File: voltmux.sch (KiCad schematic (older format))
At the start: 32 parts, among them J2 Conn_02x07_Counter_Clockwise, U10 CD74HC4067SM

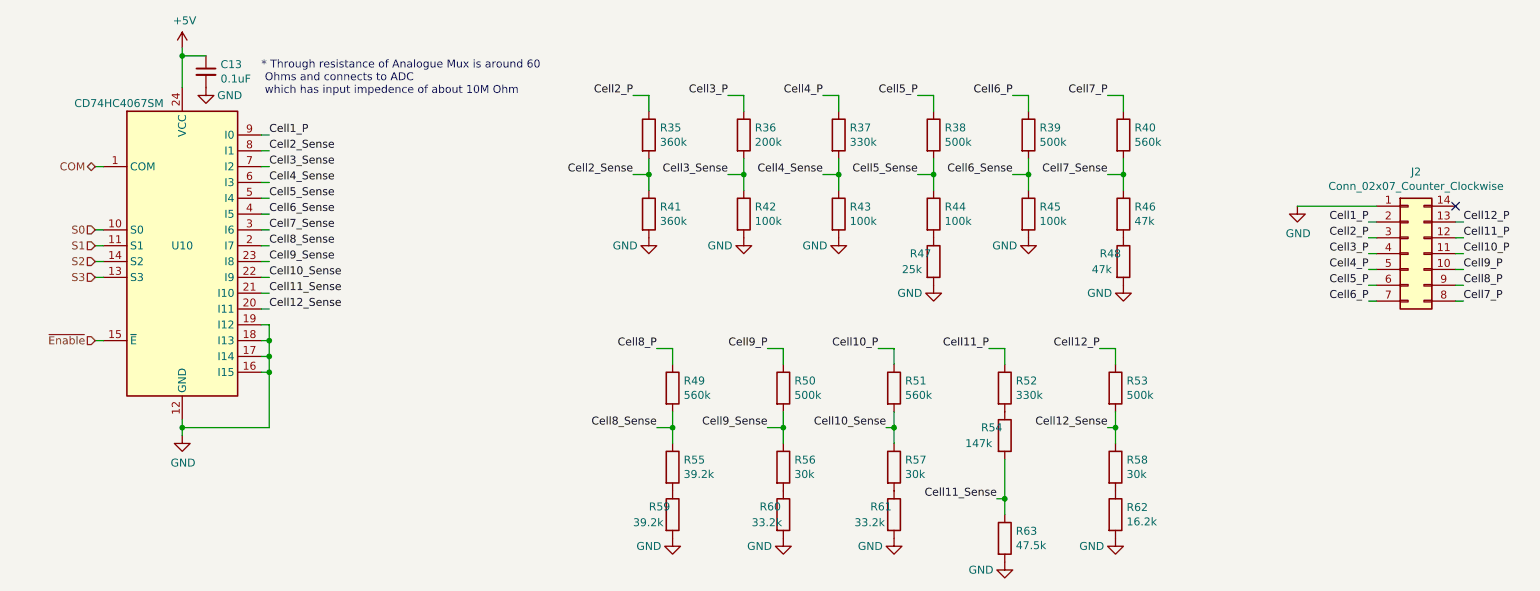
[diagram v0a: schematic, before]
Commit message: Switched to lower GPIO pin part to save space
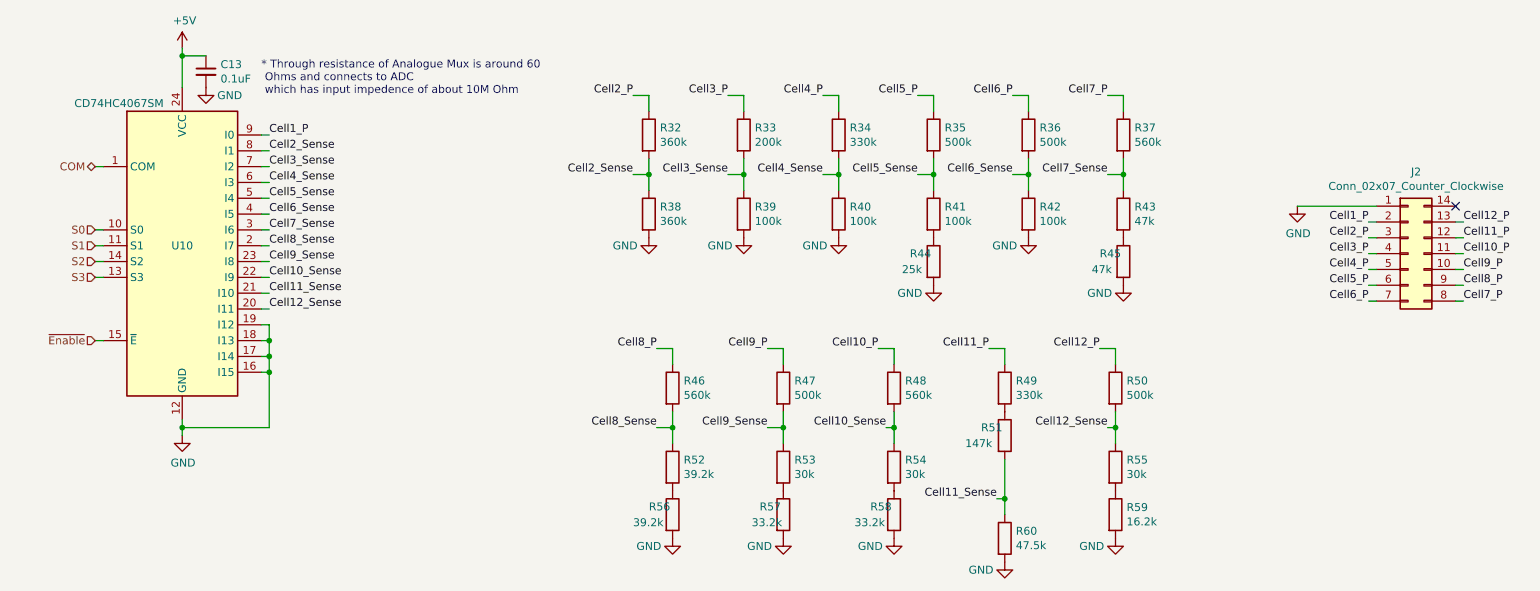
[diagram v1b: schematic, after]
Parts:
- renumbered R35 to R32, R36 to R33, R37 to R34, R38 to R35, R39 to R36, R40 to R37, R41 to R38, R42 to R39, R43 to R40, R44 to R41, R45 to R42, R46 to R43, R47 to R44, R48 to R45, R49 to R46, R50 to R47, R51 to R48, R52 to R49, R53 to R50, R54 to R51, R55 to R52, R56 to R53, R57 to R54, R58 to R55, R59 to R56, R60 to R57, R61 to R58, R62 to R59, R63 to R60

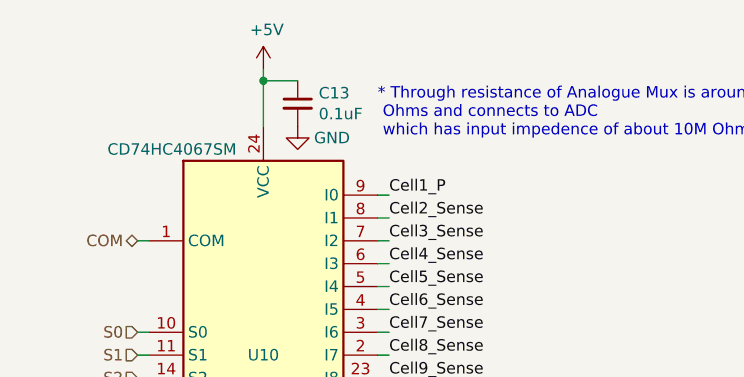
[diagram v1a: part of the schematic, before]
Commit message: Removed SD card Adapter, added programming port
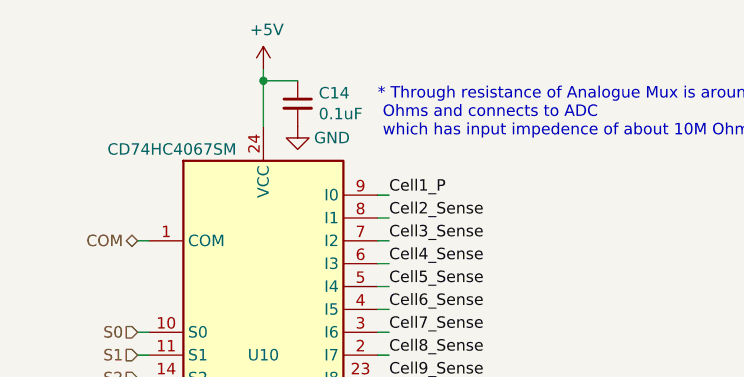
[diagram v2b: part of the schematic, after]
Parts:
- renumbered C13 to C14
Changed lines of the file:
@@
 	2350 3550 2350 3500
 $Comp
-L Device:C_Small C13
+L Device:C_Small C14
 U 1 1 5F5548EC
 P 2500 1250
-F 0 "C13" H 2592 1296 50  0000 L CNN
+F 0 "C14" H 2592 1296 50  0000 L CNN
 F 1 "0.1uF" H 2592 1205 50  0000 L CNN
 F 2 "Capacitor_SMD:C_1206_3216Metric" H 2500 1250 50  0001 C CNN

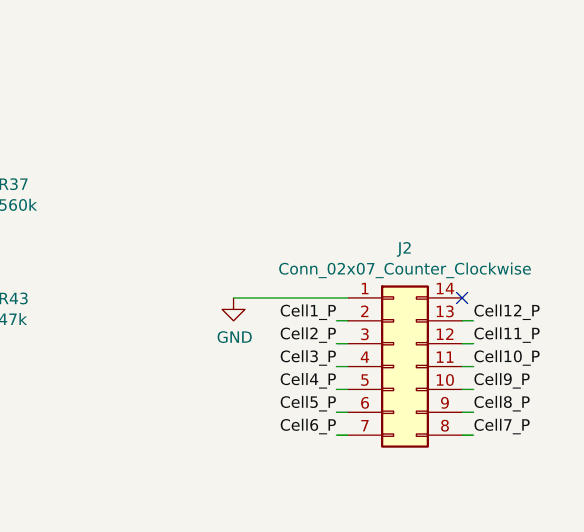
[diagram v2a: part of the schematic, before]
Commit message: Added ext ADC pin and fixed connection bugs
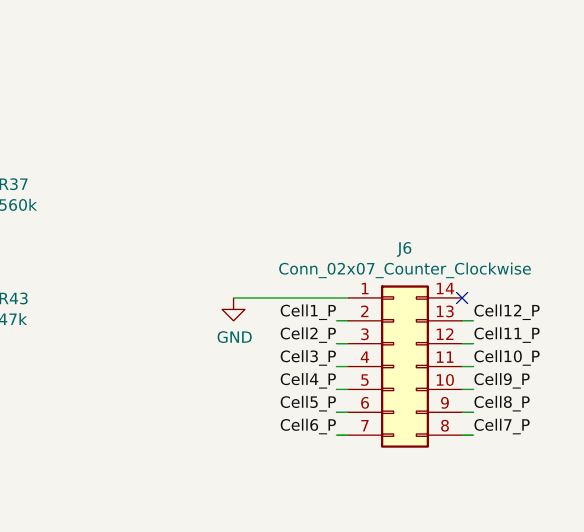
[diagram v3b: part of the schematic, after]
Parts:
- renumbered J2 to J6
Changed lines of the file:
@@
 $EndComp
 $Comp
-L power:GND #PWR055
+L power:GND #PWR057
 U 1 1 5F55349E
 P 2350 3550
-F 0 "#PWR055" H 2350 3300 50  0001 C CNN
+F 0 "#PWR057" H 2350 3300 50  0001 C CNN
 F 1 "GND" H 2355 3377 50  0000 C CNN
 F 2 "" H 2350 3550 50  0001 C CNN
@@
 $EndComp
 $Comp
-L power:GND #PWR047
+L power:GND #PWR049
 U 1 1 5F55509A
 P 2500 1350
-F 0 "#PWR047" H 2500 1100 50  0001 C CNN
+F 0 "#PWR049" H 2500 1100 50  0001 C CNN
 F 1 "GND" H 2650 1300 50  0000 C CNN
 F 2 "" H 2500 1350 50  0001 C CNN
@@
 $EndComp
 $Comp
-L power:+5V #PWR046
+L power:+5V #PWR048
 U 1 1 5F55562D
 P 2350 1100
-F 0 "#PWR046" H 2350 950 50  0001 C CNN
+F 0 "#PWR048" H 2350 950 50  0001 C CNN
 F 1 "+5V" H 2365 1273 50  0000 C CNN
 F 2 "" H 2350 1100 50  0001 C CNN
@@
 	2350 1150 2350 1350
 $Comp
-L power:GND #PWR048
+L power:GND #PWR050
 U 1 1 5F55CE43
 P 9400 2100
-F 0 "#PWR048" H 9400 1850 50  0001 C CNN
+F 0 "#PWR050" H 9400 1850 50  0001 C CNN
 F 1 "GND" H 9405 1927 50  0000 C CNN
 F 2 "" H 9400 2100 50  0001 C CNN
@@
 Cell6_P
 $Comp
-L Connector_Generic:Conn_02x07_Counter_Clockwise J2
+L Connector_Generic:Conn_02x07_Counter_Clockwise J6
 U 1 1 5F55EF88
 P 10100 2400
-F 0 "J2" H 10150 2917 50  0000 C CNN
+F 0 "J6" H 10150 2917 50  0000 C CNN
 F 1 "Conn_02x07_Counter_Clockwise" H 10150 2826 50  0000 C CNN
 F 2 "Connector_PinHeader_2.54mm:PinHeader_2x07_P2.54mm_Vertical" H 10100 2400 50  0001 C CNN
@@
 	8250 3000 8250 3100
 $Comp
-L power:GND #PWR049
+L power:GND #PWR051
 U 1 1 5F58E473
 P 5300 2300
-F 0 "#PWR049" H 5300 2050 50  0001 C CNN
+F 0 "#PWR051" H 5300 2050 50  0001 C CNN
 F 1 "GND" H 5150 2250 50  0000 C CNN
 F 2 "" H 5300 2300 50  0001 C CNN
@@
 $EndComp
 $Comp
-L power:GND #PWR050
+L power:GND #PWR052
 U 1 1 5F58E961
 P 5900 2300
-F 0 "#PWR050" H 5900 2050 50  0001 C CNN
+F 0 "#PWR052" H 5900 2050 50  0001 C CNN
 F 1 "GND" H 5750 2250 50  0000 C CNN
 F 2 "" H 5900 2300 50  0001 C CNN
@@
 $EndComp
 $Comp
-L power:GND #PWR051
+L power:GND #PWR053
 U 1 1 5F58EB9B
 P 6500 2300
-F 0 "#PWR051" H 6500 2050 50  0001 C CNN
+F 0 "#PWR053" H 6500 2050 50  0001 C CNN
 F 1 "GND" H 6350 2250 50  0000 C CNN
 F 2 "" H 6500 2300 50  0001 C CNN
@@
 $EndComp
 $Comp
-L power:GND #PWR052
+L power:GND #PWR054
 U 1 1 5F58EF8D
 P 7700 2300
-F 0 "#PWR052" H 7700 2050 50  0001 C CNN
+F 0 "#PWR054" H 7700 2050 50  0001 C CNN
 F 1 "GND" H 7550 2250 50  0000 C CNN
 F 2 "" H 7700 2300 50  0001 C CNN
@@
 $EndComp
 $Comp
-L power:GND #PWR060
+L power:GND #PWR062
 U 1 1 5F58FB94
 P 7550 4350
-F 0 "#PWR060" H 7550 4100 50  0001 C CNN
+F 0 "#PWR062" H 7550 4100 50  0001 C CNN
 F 1 "GND" H 7400 4300 50  0000 C CNN
 F 2 "" H 7550 4350 50  0001 C CNN
@@
 $EndComp
 $Comp
-L power:GND #PWR058
+L power:GND #PWR060
 U 1 1 5F627115
 P 6850 4200
-F 0 "#PWR058" H 6850 3950 50  0001 C CNN
+F 0 "#PWR060" H 6850 3950 50  0001 C CNN
 F 1 "GND" H 6700 4150 50  0000 C CNN
 F 2 "" H 6850 4200 50  0001 C CNN
@@
 $EndComp
 $Comp
-L power:GND #PWR057
+L power:GND #PWR059
 U 1 1 5F6278F7
 P 6150 4200
-F 0 "#PWR057" H 6150 3950 50  0001 C CNN
+F 0 "#PWR059" H 6150 3950 50  0001 C CNN
 F 1 "GND" H 6000 4150 50  0000 C CNN
 F 2 "" H 6150 4200 50  0001 C CNN
@@
 $EndComp
 $Comp
-L power:GND #PWR056
+L power:GND #PWR058
 U 1 1 5F627F6F
 P 5450 4200
-F 0 "#PWR056" H 5450 3950 50  0001 C CNN
+F 0 "#PWR058" H 5450 3950 50  0001 C CNN
 F 1 "GND" H 5300 4150 50  0000 C CNN
 F 2 "" H 5450 4200 50  0001 C CNN
@@
 $EndComp
 $Comp
-L power:GND #PWR059
+L power:GND #PWR061
 U 1 1 5F638E0E
 P 8250 4200
-F 0 "#PWR059" H 8250 3950 50  0001 C CNN
+F 0 "#PWR061" H 8250 3950 50  0001 C CNN
 F 1 "GND" H 8100 4150 50  0000 C CNN
 F 2 "" H 8250 4200 50  0001 C CNN
@@
 Connection ~ 7550 3950
 $Comp
-L power:GND #PWR053
+L power:GND #PWR055
 U 1 1 5F6490F9
 P 7100 2600
-F 0 "#PWR053" H 7100 2350 50  0001 C CNN
+F 0 "#PWR055" H 7100 2350 50  0001 C CNN
 F 1 "GND" H 6950 2550 50  0000 C CNN
 F 2 "" H 7100 2600 50  0001 C CNN
@@
 $EndComp
 $Comp
-L power:GND #PWR054
+L power:GND #PWR056
 U 1 1 5F64935A
 P 8300 2600
-F 0 "#PWR054" H 8300 2350 50  0001 C CNN
+F 0 "#PWR056" H 8300 2350 50  0001 C CNN
 F 1 "GND" H 8150 2550 50  0000 C CNN
 F 2 "" H 8300 2600 50  0001 C CNN

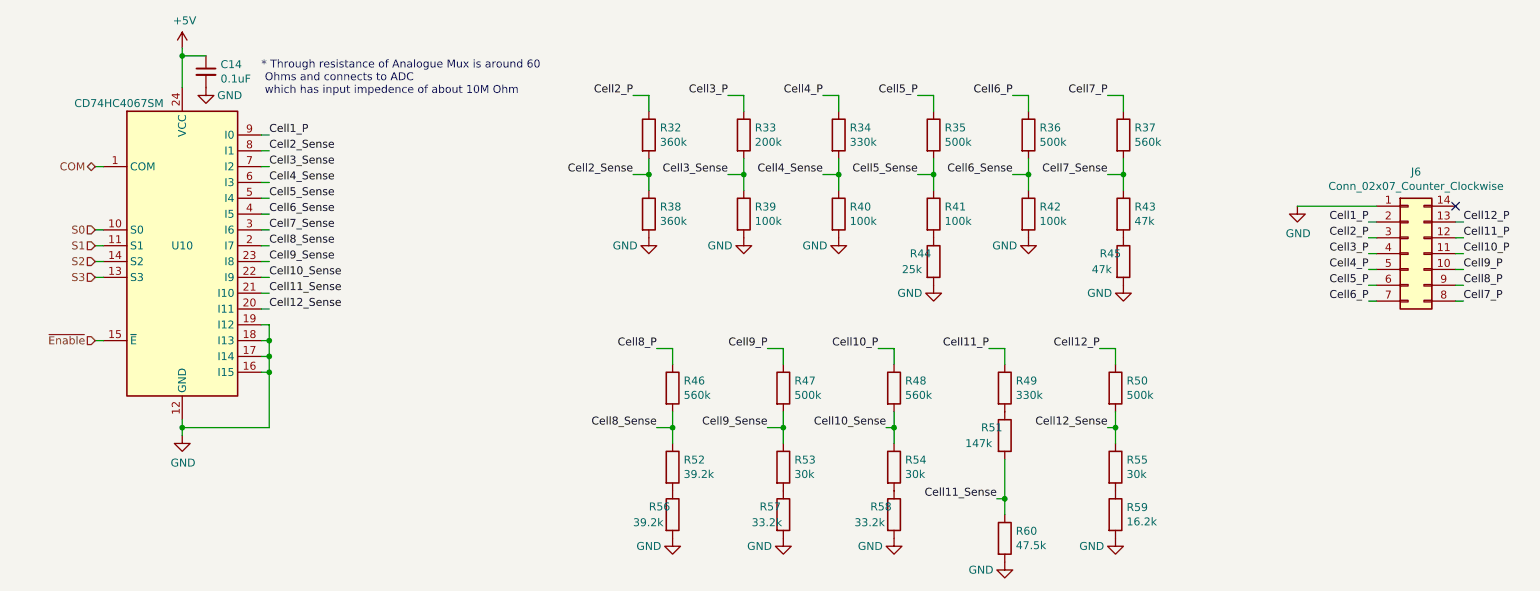
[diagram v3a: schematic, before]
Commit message: Added JST power connect and fixed some footprints
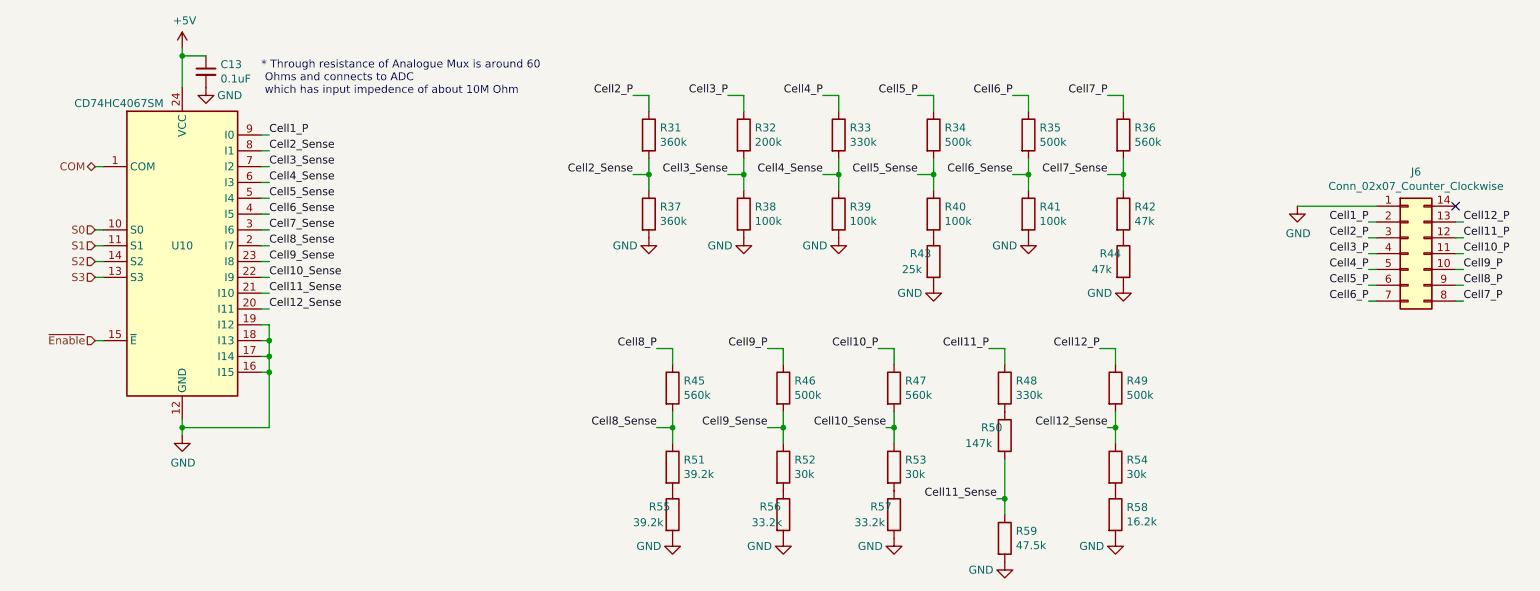
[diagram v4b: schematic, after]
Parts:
- renumbered C14 to C13, R32 to R31, R33 to R32, R34 to R33, R35 to R34, R36 to R35, R37 to R36, R38 to R37, R39 to R38, R40 to R39, R41 to R40, R42 to R41, R43 to R42, R44 to R43, R45 to R44, R46 to R45, R47 to R46, R48 to R47, R49 to R48, R50 to R49, R51 to R50, R52 to R51, R53 to R52, R54 to R53, R55 to R54, R56 to R55, R57 to R56, R58 to R57, R59 to R58, R60 to R59

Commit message: Refactored some naming
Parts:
- renumbered J6 to J5
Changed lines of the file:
@@
 $EndComp
 $Comp
-L power:GND #PWR055
+L power:GND #PWR054
 U 1 1 5F55349E
 P 2350 3550
-F 0 "#PWR055" H 2350 3300 50  0001 C CNN
+F 0 "#PWR054" H 2350 3300 50  0001 C CNN
 F 1 "GND" H 2355 3377 50  0000 C CNN
 F 2 "" H 2350 3550 50  0001 C CNN
@@
 $EndComp
 $Comp
-L power:GND #PWR047
+L power:GND #PWR046
 U 1 1 5F55509A
 P 2500 1350
-F 0 "#PWR047" H 2500 1100 50  0001 C CNN
+F 0 "#PWR046" H 2500 1100 50  0001 C CNN
 F 1 "GND" H 2650 1300 50  0000 C CNN
 F 2 "" H 2500 1350 50  0001 C CNN
@@
 $EndComp
 $Comp
-L power:+5V #PWR046
+L power:+5V #PWR045
 U 1 1 5F55562D
 P 2350 1100
-F 0 "#PWR046" H 2350 950 50  0001 C CNN
+F 0 "#PWR045" H 2350 950 50  0001 C CNN
 F 1 "+5V" H 2365 1273 50  0000 C CNN
 F 2 "" H 2350 1100 50  0001 C CNN
@@
 	2350 1150 2350 1350
 $Comp
-L power:GND #PWR048
+L power:GND #PWR047
 U 1 1 5F55CE43
 P 9400 2100
-F 0 "#PWR048" H 9400 1850 50  0001 C CNN
+F 0 "#PWR047" H 9400 1850 50  0001 C CNN
 F 1 "GND" H 9405 1927 50  0000 C CNN
 F 2 "" H 9400 2100 50  0001 C CNN
@@
 Cell6_P
 $Comp
-L Connector_Generic:Conn_02x07_Counter_Clockwise J6
+L Connector_Generic:Conn_02x07_Counter_Clockwise J5
 U 1 1 5F55EF88
 P 10100 2400
-F 0 "J6" H 10150 2917 50  0000 C CNN
+F 0 "J5" H 10150 2917 50  0000 C CNN
 F 1 "Conn_02x07_Counter_Clockwise" H 10150 2826 50  0000 C CNN
 F 2 "Connector_PinHeader_2.54mm:PinHeader_2x07_P2.54mm_Vertical" H 10100 2400 50  0001 C CNN
@@
 	8250 3000 8250 3100
 $Comp
-L power:GND #PWR049
+L power:GND #PWR048
 U 1 1 5F58E473
 P 5300 2300
-F 0 "#PWR049" H 5300 2050 50  0001 C CNN
+F 0 "#PWR048" H 5300 2050 50  0001 C CNN
 F 1 "GND" H 5150 2250 50  0000 C CNN
 F 2 "" H 5300 2300 50  0001 C CNN
@@
 $EndComp
 $Comp
-L power:GND #PWR050
+L power:GND #PWR049
 U 1 1 5F58E961
 P 5900 2300
-F 0 "#PWR050" H 5900 2050 50  0001 C CNN
+F 0 "#PWR049" H 5900 2050 50  0001 C CNN
 F 1 "GND" H 5750 2250 50  0000 C CNN
 F 2 "" H 5900 2300 50  0001 C CNN
@@
 $EndComp
 $Comp
-L power:GND #PWR051
+L power:GND #PWR050
 U 1 1 5F58EB9B
 P 6500 2300
-F 0 "#PWR051" H 6500 2050 50  0001 C CNN
+F 0 "#PWR050" H 6500 2050 50  0001 C CNN
 F 1 "GND" H 6350 2250 50  0000 C CNN
 F 2 "" H 6500 2300 50  0001 C CNN
@@
 $EndComp
 $Comp
-L power:GND #PWR052
+L power:GND #PWR051
 U 1 1 5F58EF8D
 P 7700 2300
-F 0 "#PWR052" H 7700 2050 50  0001 C CNN
+F 0 "#PWR051" H 7700 2050 50  0001 C CNN
 F 1 "GND" H 7550 2250 50  0000 C CNN
 F 2 "" H 7700 2300 50  0001 C CNN
@@
 $EndComp
 $Comp
-L power:GND #PWR060
+L power:GND #PWR059
 U 1 1 5F58FB94
 P 7550 4350
-F 0 "#PWR060" H 7550 4100 50  0001 C CNN
+F 0 "#PWR059" H 7550 4100 50  0001 C CNN
 F 1 "GND" H 7400 4300 50  0000 C CNN
 F 2 "" H 7550 4350 50  0001 C CNN
@@
 $EndComp
 $Comp
-L power:GND #PWR058
+L power:GND #PWR057
 U 1 1 5F627115
 P 6850 4200
-F 0 "#PWR058" H 6850 3950 50  0001 C CNN
+F 0 "#PWR057" H 6850 3950 50  0001 C CNN
 F 1 "GND" H 6700 4150 50  0000 C CNN
 F 2 "" H 6850 4200 50  0001 C CNN
@@
 $EndComp
 $Comp
-L power:GND #PWR057
+L power:GND #PWR056
 U 1 1 5F6278F7
 P 6150 4200
-F 0 "#PWR057" H 6150 3950 50  0001 C CNN
+F 0 "#PWR056" H 6150 3950 50  0001 C CNN
 F 1 "GND" H 6000 4150 50  0000 C CNN
 F 2 "" H 6150 4200 50  0001 C CNN
@@
 $EndComp
 $Comp
-L power:GND #PWR056
+L power:GND #PWR055
 U 1 1 5F627F6F
 P 5450 4200
-F 0 "#PWR056" H 5450 3950 50  0001 C CNN
+F 0 "#PWR055" H 5450 3950 50  0001 C CNN
 F 1 "GND" H 5300 4150 50  0000 C CNN
 F 2 "" H 5450 4200 50  0001 C CNN
@@
 $EndComp
 $Comp
-L power:GND #PWR059
+L power:GND #PWR058
 U 1 1 5F638E0E
 P 8250 4200
-F 0 "#PWR059" H 8250 3950 50  0001 C CNN
+F 0 "#PWR058" H 8250 3950 50  0001 C CNN
 F 1 "GND" H 8100 4150 50  0000 C CNN
 F 2 "" H 8250 4200 50  0001 C CNN
@@
 Connection ~ 7550 3950
 $Comp
-L power:GND #PWR053
+L power:GND #PWR052
 U 1 1 5F6490F9
 P 7100 2600
-F 0 "#PWR053" H 7100 2350 50  0001 C CNN
+F 0 "#PWR052" H 7100 2350 50  0001 C CNN
 F 1 "GND" H 6950 2550 50  0000 C CNN
 F 2 "" H 7100 2600 50  0001 C CNN
@@
 $EndComp
 $Comp
-L power:GND #PWR054
+L power:GND #PWR053
 U 1 1 5F64935A
 P 8300 2600
-F 0 "#PWR054" H 8300 2350 50  0001 C CNN
+F 0 "#PWR053" H 8300 2350 50  0001 C CNN
 F 1 "GND" H 8150 2550 50  0000 C CNN
 F 2 "" H 8300 2600 50  0001 C CNN

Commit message: Added new 14 pin connector footprint
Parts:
- J5: footprint Connector_PinHeader_2.54mm:PinHeader_2x07_P2.54mm_Vertical -> uBMS-2:CNC-Tech_3020-14-0300-00
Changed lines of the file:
@@
 F 0 "J5" H 10150 2917 50  0000 C CNN
 F 1 "Conn_02x07_Counter_Clockwise" H 10150 2826 50  0000 C CNN
-F 2 "Connector_PinHeader_2.54mm:PinHeader_2x07_P2.54mm_Vertical" H 10100 2400 50  0001 C CNN
+F 2 "uBMS-2:CNC-Tech_3020-14-0300-00" H 10100 2400 50  0001 C CNN
 F 3 "~" H 10100 2400 50  0001 C CNN
 	1    10100 2400

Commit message: Using Molex Milli Grid Connector for 14 pin
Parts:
- J5: footprint uBMS-2:CNC-Tech_3020-14-0300-00 -> uBMS-2:Molex_Milli_Grid_0878325623
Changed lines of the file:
@@
 F 0 "J5" H 10150 2917 50  0000 C CNN
 F 1 "Conn_02x07_Counter_Clockwise" H 10150 2826 50  0000 C CNN
-F 2 "uBMS-2:CNC-Tech_3020-14-0300-00" H 10100 2400 50  0001 C CNN
+F 2 "uBMS-2:Molex_Milli_Grid_0878325623" H 10100 2400 50  0001 C CNN
 F 3 "~" H 10100 2400 50  0001 C CNN
 	1    10100 2400

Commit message: routed and filled a bunch of stuff, so much more to do
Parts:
- removed J5: Conn_02x07_Counter_Clockwise, uBMS-2:Molex_Milli_Grid_0878325623, symbol Connector_Generic:Conn_02x07_Counter_Clockwise
- added J5: Conn_02x07_Odd_Even, uBMS-2:Molex_Milli_Grid_0878325623_TopBottom, symbol Connector_Generic:Conn_02x07_Odd_Even
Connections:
- net Cell10_P: now also J5.11 (Pin_11)
- net Cell11_P: now also J5.12 (Pin_12)
- net Cell12_P: now also J5.13 (Pin_13)
- net Cell1_P: now also J5.2 (Pin_2)
- net Cell2_P: now also J5.3 (Pin_3)
- net Cell3_P: now also J5.4 (Pin_4)
- net Cell4_P: now also J5.5 (Pin_5)
- net Cell5_P: now also J5.6 (Pin_6)
- net Cell6_P: now also J5.7 (Pin_7)
- net Cell7_P: now also J5.8 (Pin_8)
- net Cell8_P: now also J5.9 (Pin_9)
- net Cell9_P: now also J5.10 (Pin_10)
- net GND: now also J5.1 (Pin_1)
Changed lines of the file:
@@
 	1    0    0    -1
 $EndComp
+Text Label 10450 2100 0    50   ~ 0
+Cell1_P
 Text Label 9850 2200 2    50   ~ 0
-Cell1_P
+Cell2_P
+Text Label 10450 2200 0    50   ~ 0
+Cell3_P
 Text Label 9850 2300 2    50   ~ 0
-Cell2_P
+Cell4_P
+Text Label 10450 2300 0    50   ~ 0
+Cell5_P
 Text Label 9850 2400 2    50   ~ 0
-Cell3_P
+Cell6_P
+Wire Wire Line
+	9400 2100 9900 2100
+Text Label 10450 2400 0    50   ~ 0
+Cell7_P
 Text Label 9850 2500 2    50   ~ 0
-Cell4_P
-Text Label 9850 2600 2    50   ~ 0
-Cell5_P
-Text Label 9850 2700 2    50   ~ 0
-Cell6_P
-$Comp
-L Connector_Generic:Conn_02x07_Counter_Clockwise J5
-U 1 1 5F55EF88
-P 10100 2400
-F 0 "J5" H 10150 2917 50  0000 C CNN
-F 1 "Conn_02x07_Counter_Clockwise" H 10150 2826 50  0000 C CNN
-F 2 "uBMS-2:Molex_Milli_Grid_0878325623" H 10100 2400 50  0001 C CNN
-F 3 "~" H 10100 2400 50  0001 C CNN
-	1    10100 2400
-	1    0    0    -1
-$EndComp
-Wire Wire Line
-	9400 2100 9900 2100
-Text Label 10450 2700 0    50   ~ 0
-Cell7_P
-Text Label 10450 2600 0    50   ~ 0
 Cell8_P
 Text Label 10450 2500 0    50   ~ 0
 Cell9_P
-Text Label 10450 2400 0    50   ~ 0
+Text Label 9850 2600 2    50   ~ 0
 Cell10_P
-Text Label 10450 2300 0    50   ~ 0
+Text Label 10450 2600 0    50   ~ 0
 Cell11_P
-Text Label 10450 2200 0    50   ~ 0
+Text Label 9850 2700 2    50   ~ 0
 Cell12_P
 Wire Wire Line
@@
 Wire Wire Line
 	10450 2200 10400 2200
-NoConn ~ 10400 2100
 Text Label 2900 1650 0    50   ~ 0
 Cell1_P
@@
 Wire Wire Line
 	1800 2950 1850 2950
+$Comp
+L Connector_Generic:Conn_02x07_Odd_Even J5
+U 1 1 5F37E464
+P 10100 2400
+F 0 "J5" H 10150 2917 50  0000 C CNN
+F 1 "Conn_02x07_Odd_Even" H 10150 2826 50  0000 C CNN
+F 2 "uBMS-2:Molex_Milli_Grid_0878325623_TopBottom" H 10100 2400 50  0001 C CNN
+F 3 "~" H 10100 2400 50  0001 C CNN
+	1    10100 2400
+	1    0    0    -1
+$EndComp
+Wire Wire Line
+	10450 2100 10400 2100
+NoConn ~ 10450 2700
 $EndSCHEMATC
